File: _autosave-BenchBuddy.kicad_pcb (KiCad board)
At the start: 4 copper layers, 165.1 x 63.5 mm, 125 parts, among them K1 1461069-5, P1 24 Pin MiniFit JR, P2 CONN_3X2, P3 CONN_2, P4 12 Pin Terminal Block, P5 3 Pin TB, Q1 2N3904, Q2 DMN65D8L-7, Q3 AOD476, Q4 AOD476, SW1 Power Switch, U1 LTV-816S, U11 LM317, U2 MCP3901, U3 LMT84, U4 OPA4170, U5 MCP4801, U6 LM337T, U7 AP5726, U8 LM337T, U9 LM317

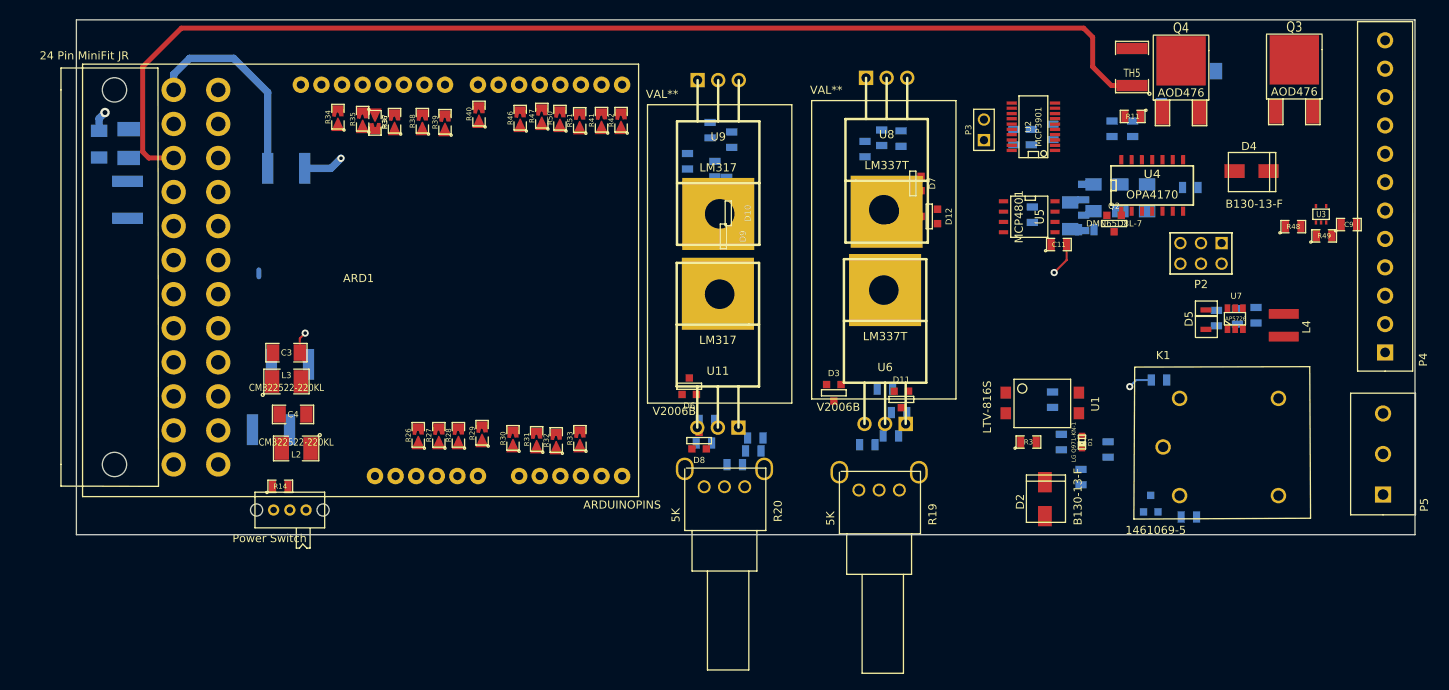
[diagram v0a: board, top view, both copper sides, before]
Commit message: More ground plane changes
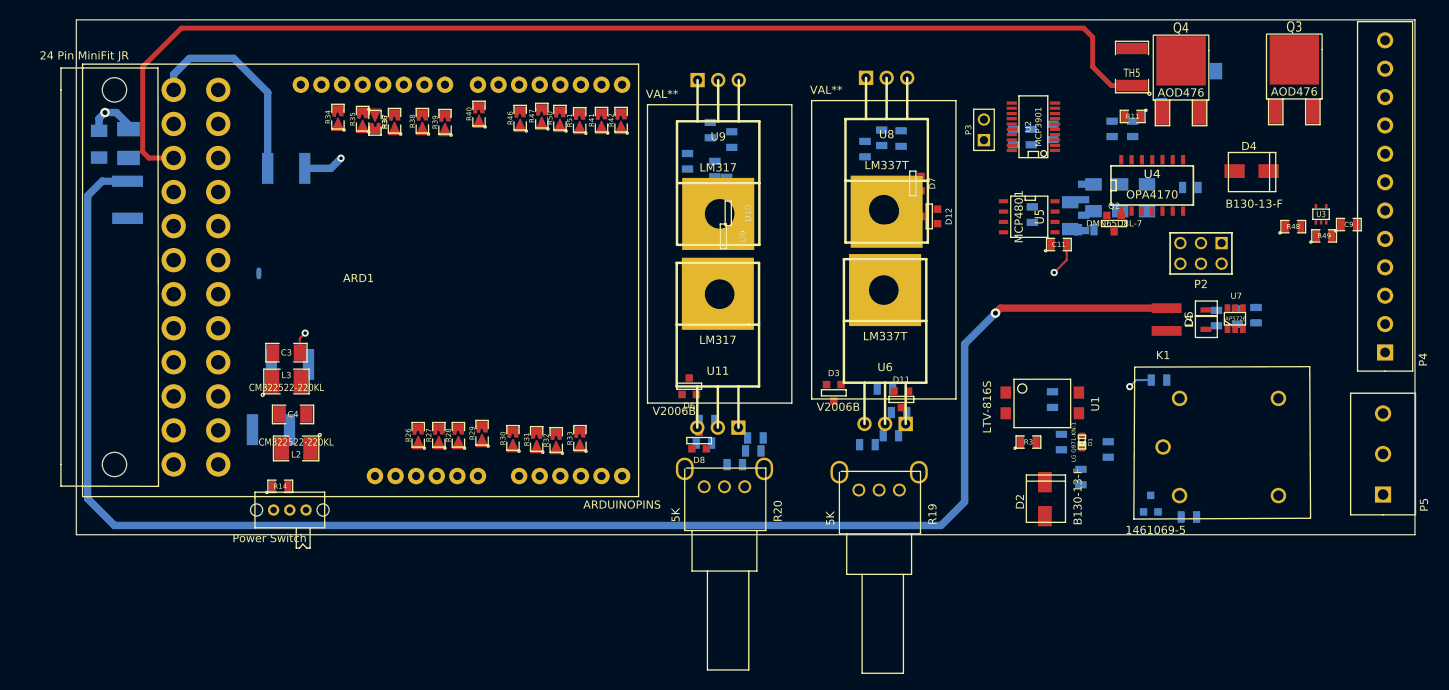
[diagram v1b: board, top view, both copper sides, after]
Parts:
- moved L4 14.5 mm to (270.7, 131.3)
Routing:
- net +5P: track 0.00 -> 200.0 mm, vias 0 -> 1
- net +5V: track 2.55 -> 6.62 mm
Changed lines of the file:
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@@
   (general
     (links 326)
-    (no_connects 299)
+    (no_connects 297)
     (area 136.195999 95.682999 301.446001 159.333001)
     (thickness 1.6)
     (drawings 4)
-    (tracks 39)
+    (tracks 53)
     (zones 0)
     (modules 125)
@@
   (layers
     (15 F.Cu signal)
-    (2 PWR power)
-    (1 GND power hide)
+    (2 PWR power hide)
+    (1 GND power)
     (0 B.Cu signal)
     (16 B.Adhes user)
@@
   )
   (module NR4012 (layer F.Cu)
-    (at 285.1912 132.0292 270)
+    (at 270.7386 131.318 270)
     (fp_text reference L4 (at 1.6 -2.8 270) (layer F.SilkS)
       (effects (font (size 1 1) (thickness 0.15)))
@@
   (via (at 168.91 112.8268) (size 0.889) (layers F.Cu B.Cu) (net 4))
   (segment (start 167.6654 114.0714) (end 168.91 112.8268) (width 0.9144) (layer B.Cu) (net 4))
-  (segment (start 139.0777 109.4359) (end 139.0777 107.9119) (width 0.9144) (layer B.Cu) (net 6) (status 400000))
-  (via (at 139.8016 107.188) (size 1.1684) (drill 0.6096) (layers F.Cu B.Cu) (net 6))
+  (segment (start 142.5829 115.6589) (end 139.4587 115.6589) (width 0.9144) (layer B.Cu) (net 5) (status 400000))
+  (segment (start 250.2408 131.318) (end 270.7386 131.318) (width 0.9144) (layer F.Cu) (net 5) (status 800000))
+  (segment (start 249.6312 131.9276) (end 250.2408 131.318) (width 0.9144) (layer F.Cu) (net 5))
+  (via (at 249.6312 131.9276) (size 1.1684) (drill 0.6096) (layers F.Cu B.Cu) (net 5))
+  (segment (start 245.8212 135.7376) (end 249.6312 131.9276) (width 0.9144) (layer B.Cu) (net 5))
+  (segment (start 245.8212 155.2194) (end 245.8212 135.7376) (width 0.9144) (layer B.Cu) (net 5))
+  (segment (start 242.9256 158.115) (end 245.8212 155.2194) (width 0.9144) (layer B.Cu) (net 5))
+  (segment (start 140.97 158.115) (end 242.9256 158.115) (width 0.9144) (layer B.Cu) (net 5))
+  (segment (start 137.668 154.813) (end 140.97 158.115) (width 0.9144) (layer B.Cu) (net 5))
+  (segment (start 137.668 117.4496) (end 137.668 154.813) (width 0.9144) (layer B.Cu) (net 5))
+  (segment (start 139.4587 115.6589) (end 137.668 117.4496) (width 0.9144) (layer B.Cu) (net 5))
+  (segment (start 142.7099 109.2327) (end 142.7099 108.6993) (width 0.9144) (layer B.Cu) (net 6))
   (segment (start 139.0777 107.9119) (end 139.8016 107.188) (width 0.9144) (layer B.Cu) (net 6))
+  (via (at 139.8016 107.188) (size 1.1684) (drill 0.6096) (layers F.Cu B.Cu) (net 6))
+  (segment (start 139.0777 107.9119) (end 139.0777 109.4359) (width 0.9144) (layer B.Cu) (net 6))
+  (segment (start 141.1986 107.188) (end 139.8016 107.188) (width 0.9144) (layer B.Cu) (net 6))
+  (segment (start 142.7099 108.6993) (end 141.1986 107.188) (width 0.9144) (layer B.Cu) (net 6))
   (segment (start 258.4069 123.4694) (end 258.4069 125.3871) (width 0.254) (layer F.Cu) (net 42))
   (segment (start 256.8194 126.9746) (end 256.7178 126.9746) (width 0.254) (layer GND) (net 42))
